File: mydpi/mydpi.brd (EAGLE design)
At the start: 40 x 20 mm, 16 parts, among them Q1 DMN3404L, U1 MEGA32U4-MU, U2 AP7381-33Y-13

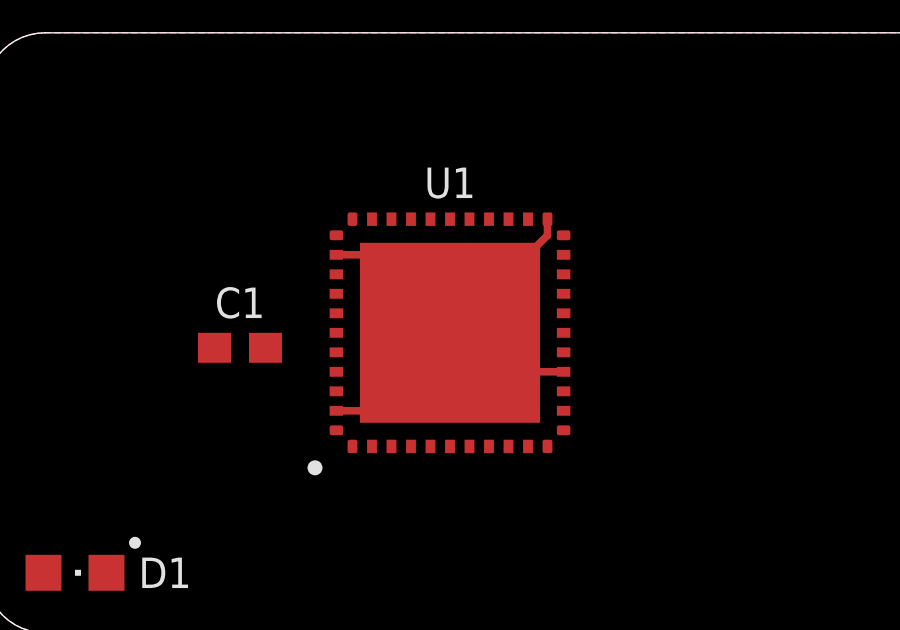
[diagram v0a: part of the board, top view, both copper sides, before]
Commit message: Added supply voltage
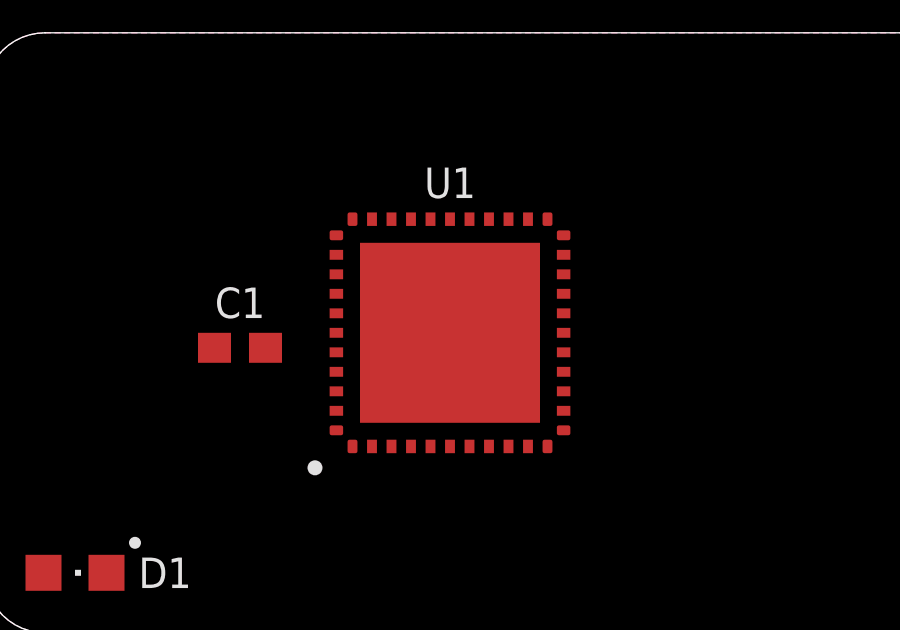
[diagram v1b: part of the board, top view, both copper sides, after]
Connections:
- new net +5V: D1.A
- new net N$1: R3.1, U1.32
- new net N$2: D1.C, R3.2
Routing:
- net GND: track 5.81 -> 0.00 mm
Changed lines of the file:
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@@
 <drawing>
 <settings>
-<setting alwaysvectorfont="yes"/>
+<setting alwaysvectorfont="no"/>
 <setting verticaltext="up"/>
 </settings>
@@
 </signal>
 <signal name="GND">
-<contactref element="U1" pad="23"/>
-<contactref element="U1" pad="15"/>
-<contactref element="U1" pad="EXP"/>
-<contactref element="U1" pad="35"/>
-<contactref element="U1" pad="43"/>
 <polygon width="0.254" layer="16">
 <vertex x="2" y="20"/>
@@
 <vertex x="0" y="18" curve="-90"/>
 </polygon>
-<wire x1="11.7125" y1="12.6" x2="12.9" y2="12.6" width="0.254" layer="1"/>
-<wire x1="12.9" y1="12.6" x2="13" y2="12.5" width="0.254" layer="1"/>
-<wire x1="11.7125" y1="7.4" x2="12.9" y2="7.4" width="0.254" layer="1"/>
-<wire x1="12.9" y1="7.4" x2="13" y2="7.5" width="0.254" layer="1"/>
-<wire x1="19.2875" y1="8.7" x2="17.8" y2="8.7" width="0.254" layer="1"/>
-<wire x1="17.8" y1="8.7" x2="17.5" y2="9" width="0.254" layer="1"/>
-<wire x1="18.75" y1="13.7875" x2="18.75" y2="13.25" width="0.254" layer="1"/>
-<wire x1="18.75" y1="13.25" x2="18.25" y2="12.75" width="0.254" layer="1"/>
 <contactref element="U2" pad="2"/>
 <contactref element="U2" pad="2@1"/>
+<contactref element="U1" pad="15"/>
+<contactref element="U1" pad="EXP"/>
+<contactref element="U1" pad="23"/>
+<contactref element="U1" pad="35"/>
+<contactref element="U1" pad="43"/>
 <wire x1="51.5" y1="3.273" x2="51.5" y2="5.94" width="0" layer="19" extent="1-1"/>
 <wire x1="19.2875" y1="8.7" x2="51.5" y2="5.94" width="0" layer="19" extent="1-1"/>
-<wire x1="15.5" y1="10" x2="17.5" y2="9" width="0" layer="19" extent="1-1"/>
-<wire x1="13" y1="12.5" x2="15.5" y2="10" width="0" layer="19" extent="1-1"/>
-<wire x1="13" y1="7.5" x2="15.5" y2="10" width="0" layer="19" extent="1-1"/>
-<wire x1="18.25" y1="12.75" x2="17.5" y2="9" width="0" layer="19" extent="1-1"/>
+<wire x1="15.5" y1="10" x2="19.2875" y2="8.7" width="0" layer="19" extent="1-1"/>
+<wire x1="11.7125" y1="12.6" x2="15.5" y2="10" width="0" layer="19" extent="1-1"/>
+<wire x1="11.7125" y1="7.4" x2="15.5" y2="10" width="0" layer="19" extent="1-1"/>
+<wire x1="18.75" y1="13.7875" x2="15.5" y2="10" width="0" layer="19" extent="1-1"/>
 </signal>
 <signal name="VCC">
@@
 <vertex x="0" y="18" curve="-90"/>
 </polygon>
+<contactref element="D1" pad="A"/>
 </signal>
 <signal name="UCAP">
@@
 <contactref element="U1" pad="4"/>
 </signal>
+<signal name="N$1">
+<contactref element="U1" pad="32"/>
+<contactref element="R3" pad="1"/>
+<wire x1="12.9" y1="13.7875" x2="41.65" y2="36" width="0" layer="19" extent="1-1"/>
+</signal>
+<signal name="N$2">
+<contactref element="R3" pad="2"/>
+<contactref element="D1" pad="C"/>
+<wire x1="4.05" y1="2" x2="43.35" y2="36" width="0" layer="19" extent="1-1"/>
+</signal>
 </signals>

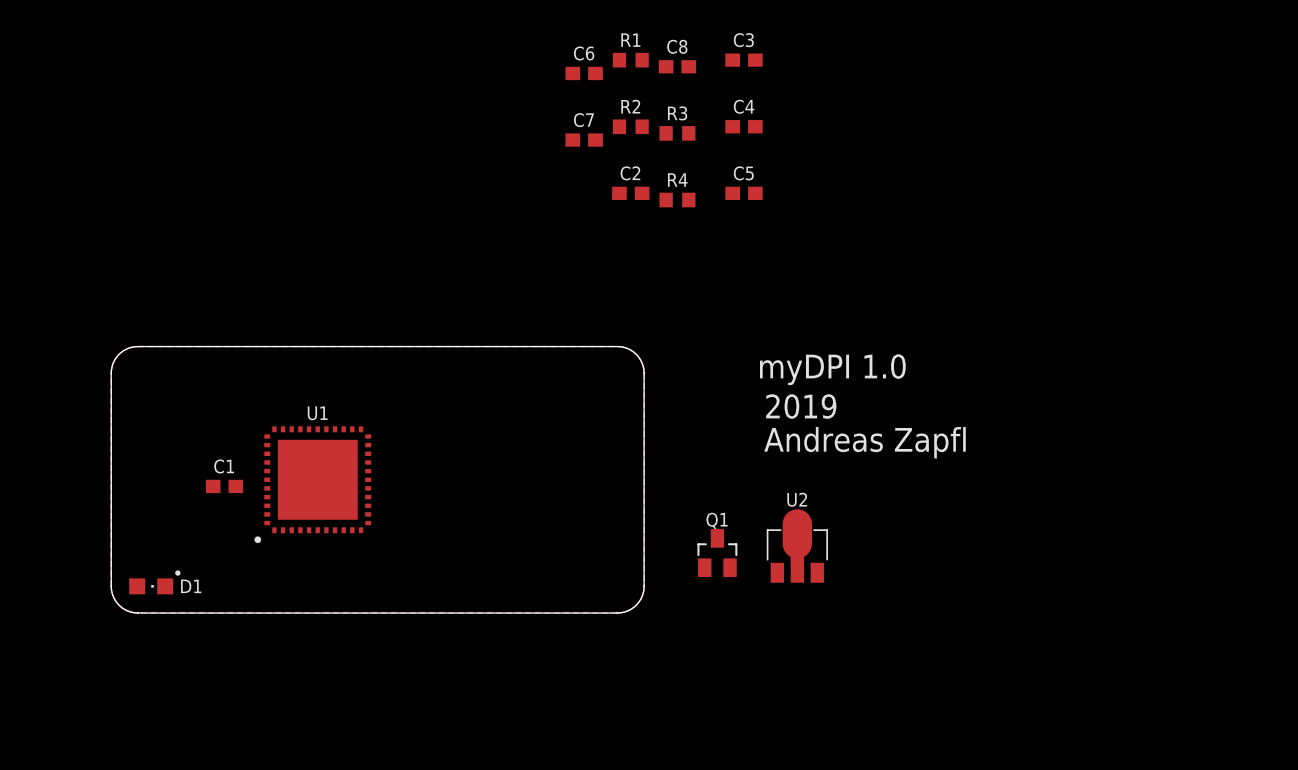
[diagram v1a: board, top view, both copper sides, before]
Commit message: CC resistors added
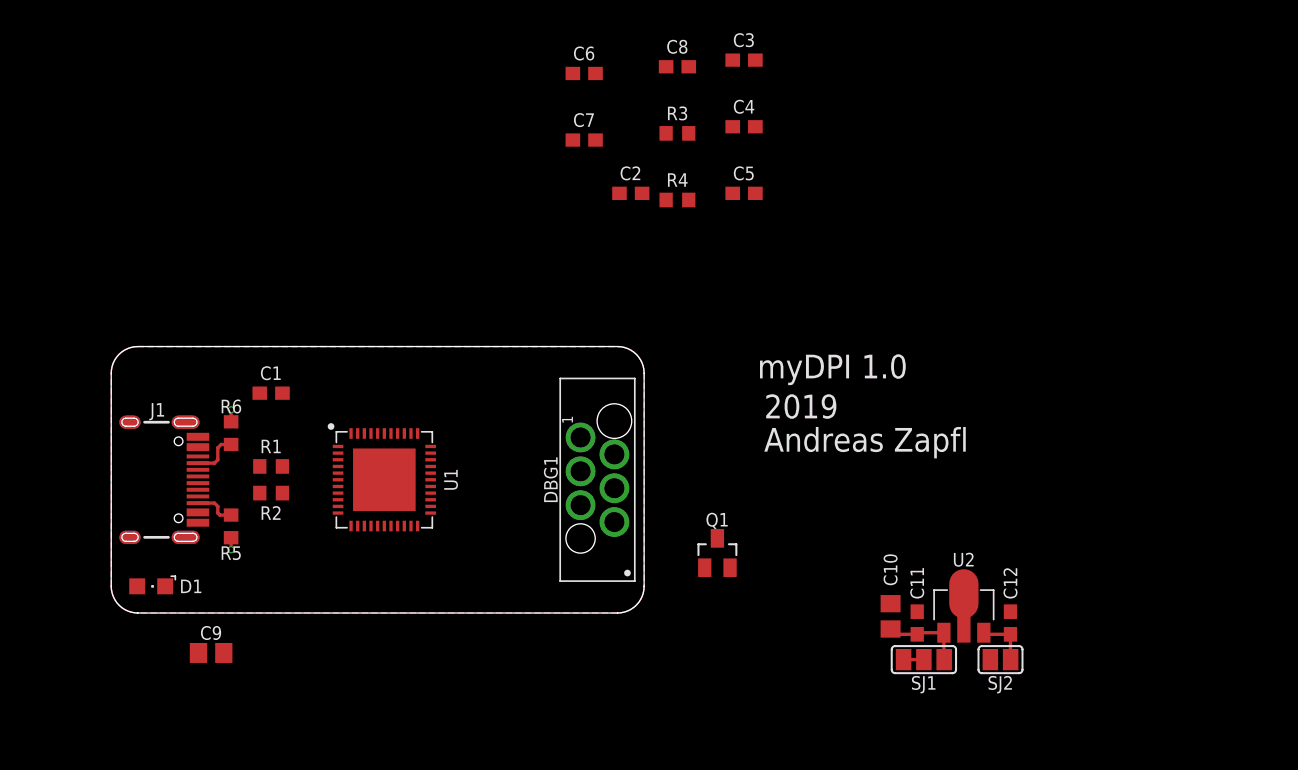
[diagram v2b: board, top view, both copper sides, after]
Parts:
- added C10, C9: 22u, zaan-Capacitors:C0805
- added C11, C12: 100n, zaan-Capacitors:C0603
- added DBG1: AVR-UPDI-SKEDD, zaan-Connectors:490107670612A
- added J1: (no value), zaan-Connectors:USB-C-16P
- added R5, R6: 5.1k, zaan-Resistors:R0603
- added SJ1: (no value), jumper:SJ_2
- added SJ2: (no value), jumper:SJ
- U1: device zaan-IC-Microcontroller:QFN44ML8X8 -> zaan-IC-Microcontroller:TQFN44_7MM
- moved R1 40.7 mm to (12.0, 11.0)
- moved R2 38.5 mm to (12.0, 9.00)
- moved U2 13.3 mm to (64.0, 0.50)
- moved C1 7.83 mm to (12.0, 16.5)
- moved U1 5.00 mm to (20.5, 10.0), turned to 0 degrees
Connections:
- new net +3V3: C10.1, C11.1, SJ1.1, U2.1
- new net MEDBG_UPDI: DBG1.3, U1.1
- new net MEDBG_VTG: DBG1.4, SJ1.2
- new net N$4: C12.1, SJ2.2, U2.3
- new net N$5: J1.B5, R5.2
- new net N$6: J1.A5, R6.2
- new net USB_N: J1.A7, J1.B7, R1.1
- new net USB_P: J1.A6, J1.B6, R2.1
- net +5V: now also J1.VBUS1, J1.VBUS2, SJ1.3, SJ2.1
- net D_N: now also R1.2
- net D_P: now also R2.2
- net GND: now also C10.2, C11.2, C12.2, DBG1.2, J1.GND, J1.GND2, R5.1, R6.1
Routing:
- net +3V3: track 0.00 -> 6.24 mm
- net N$4: track 0.00 -> 3.96 mm
- net N$6: track 0.00 -> 3.60 mm
- net N$5: track 0.00 -> 3.16 mm
- net GND: track 0.00 -> 1.80 mm, vias 0 -> 2
- net N$3: track 0.00 -> 1.50 mm

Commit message: Placement LDO, Caps
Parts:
- removed C8: 1n, zaan-Capacitors:C0603
- removed R4: 1k, zaan-Resistors:R0603
- removed SJ2: (no value), jumper:SJ
- added C13: 100n, zaan-Capacitors:C0603
- added D2: LTST-C171KSKT, zaan-Optoelectronics:CHIPLED_0805
- added ICSP1: AVR-ISP-1.27MM, zaan-Connectors:AVRISP-1.27
- added R7, R8: 100k, zaan-Resistors:R0603
- added R9: 1k, zaan-Resistors:R0603
- C6: value 1n -> 100n
- moved C9 77.9 mm to (72.5, 40.0)
- moved Q1 44.9 mm to (77.5, 36.0)
- moved C12 43.8 mm to (24.0, 4.75), flipped to the bottom, turned to 180 degrees
- moved U2 40.1 mm to (24.8, 8.75), flipped to the bottom
- moved C3 39.0 mm to (18.0, 16.0)
- moved C4 36.2 mm to (26.5, 7.00), turned to 270 degrees
- moved C11 33.3 mm to (28.2, 7.50), flipped to the bottom
- moved C2 31.6 mm to (22.5, 4.50), turned to 180 degrees
- moved D1 31.4 mm to (32.0, 14.0), turned to 0 degrees
- moved C6 31.2 mm to (32.0, 9.50), turned to 90 degrees
- moved C10 29.4 mm to (30.2, 8.00), flipped to the bottom
- moved SJ1 29.3 mm to (32.5, 3.50), flipped to the bottom, turned to 270 degrees
- moved C7 29.2 mm to (32.0, 6.50), turned to 90 degrees
- moved C5 28.6 mm to (23.5, 16.0), turned to 180 degrees
- moved R3 25.2 mm to (30.2, 14.0), turned to 90 degrees
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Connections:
- removed net AREF: U1.42
- removed net AVCC: U1.24, U1.44
- removed net N$4: C12.1, SJ2.2, U2.3
- removed net UCAP: U1.6
- removed net UGND: U1.5
- removed net UVCC: U1.2
- removed net VBUS: U1.7
- removed net VCC: U1.14, U1.34
- new net N$13: U1.17
- new net N$14: U1.16
- new net N$7: R7.1, U1.33
- new net N$8: C1.1, U1.6
- new net N$9: D2.A, R9.2
- new net PDI: ICSP1.4, U1.10
- new net PDO: ICSP1.1, U1.11
- new net RST: C13.1, ICSP1.5, R8.1, U1.13
- new net SCK: ICSP1.3, U1.9
- net +5V: now also C12.1, C2.1, C3.1, C4.1, C5.1, C6.1, C7.1, ICSP1.2, R7.2, R8.2, R9.1, U1.14, U1.2, U1.24, U1.34, U1.42, U1.44, U1.7, U2.3; no longer SJ2.1
- net D_N: now also R2.2; no longer R1.2
- net D_P: now also R1.2; no longer R2.2
- net GND: now also C1.2, C13.2, C2.2, C3.2, C4.2, C5.2, C6.2, C7.2, D2.C, ICSP1.6, U1.5
- net USB_N: now also R2.1; no longer R1.1
- net USB_P: now also R1.1; no longer R2.1
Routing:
- net MEDBG_VTG: track 0.00 -> 12.4 mm
- net +5V: track 0.00 -> 9.10 mm, vias 0 -> 3
- net N$4: track 3.96 -> 0.00 mm
- net GND: track 1.80 -> 5.18 mm, vias 2 -> 5
- net N$9: track 0.00 -> 2.08 mm
- net +3V3: track 6.24 -> 8.05 mm
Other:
- board text added: "3V3"
- board text added: "5V"
- board text added: "Target"

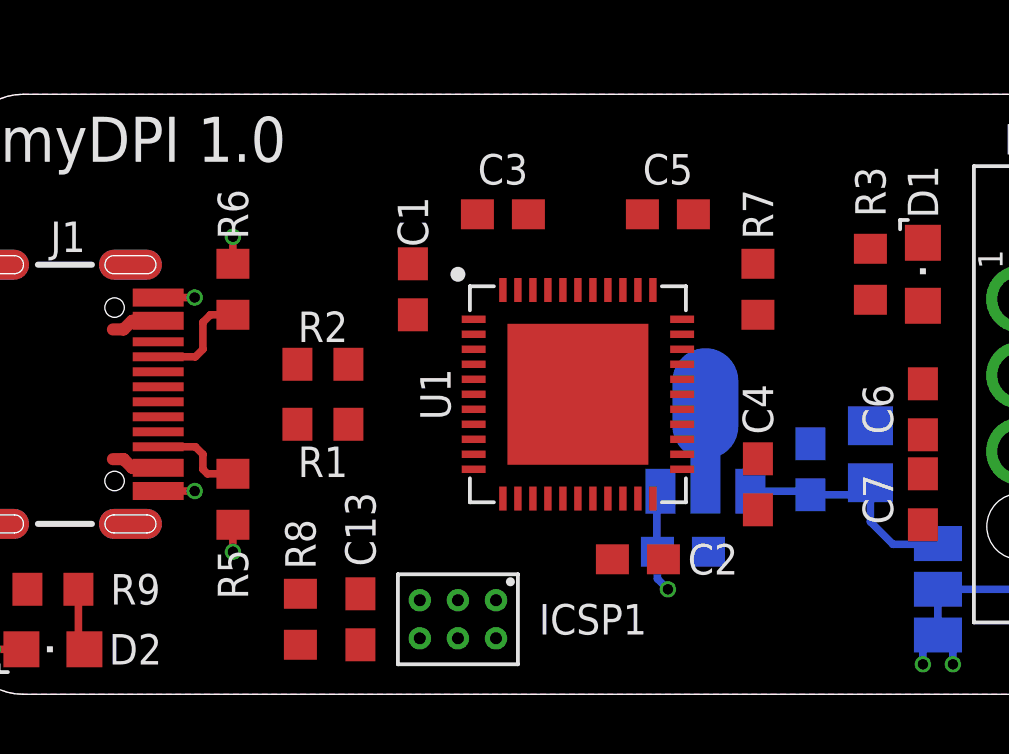
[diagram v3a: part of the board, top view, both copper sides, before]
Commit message: Crystal Added
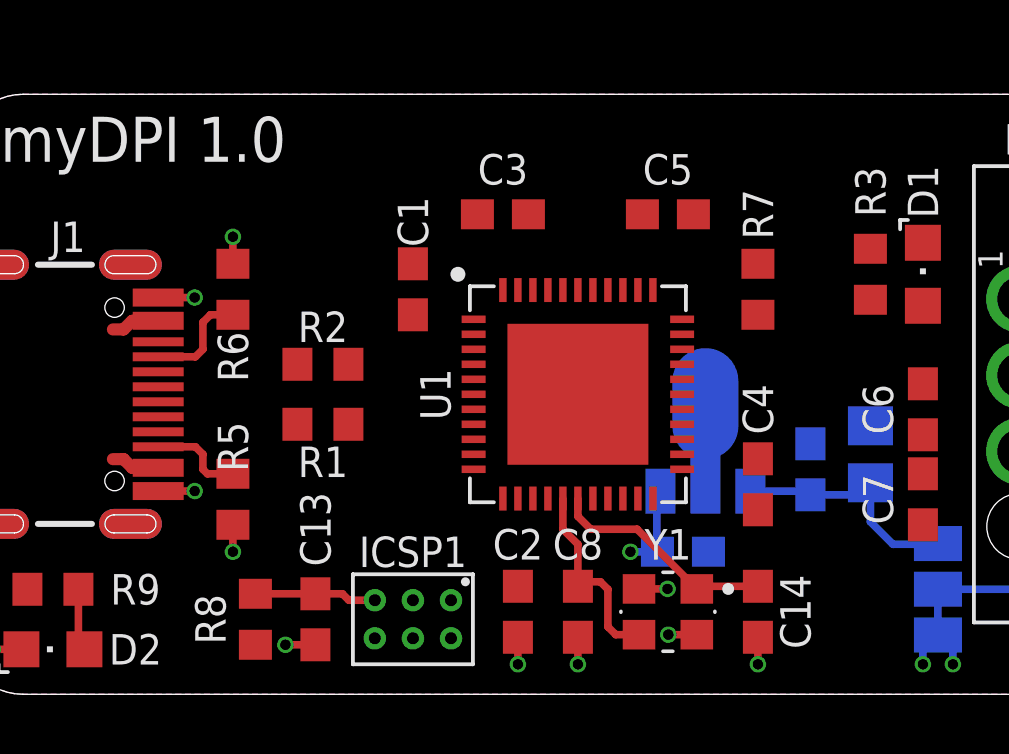
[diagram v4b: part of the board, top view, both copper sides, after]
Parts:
- added C14, C8: 12p, zaan-Capacitors:C0603
- added Y1: 830069392, zaan-Electromechanical:WE-XTAL_CFPX-218
- moved C2 4.37 mm to (18.5, 2.75), turned to 270 degrees
- moved C13 1.50 mm to (11.8, 2.50)
- moved ICSP1 1.50 mm to (15.0, 2.50)
- moved R8 1.50 mm to (9.75, 2.50)
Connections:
- removed net N$13: U1.17
- removed net N$14: U1.16
- new net XTAL1: C14.1, U1.17, Y1.1
- new net XTAL2: C8.1, U1.16, Y1.3
- net GND: now also C14.2, C8.2, Y1.2, Y1.4
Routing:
- net XTAL1: track 0.00 -> 7.77 mm
- net XTAL2: track 0.00 -> 6.63 mm
- net GND: track 5.18 -> 10.8 mm, vias 5 -> 11
- net RST: track 0.00 -> 4.07 mm

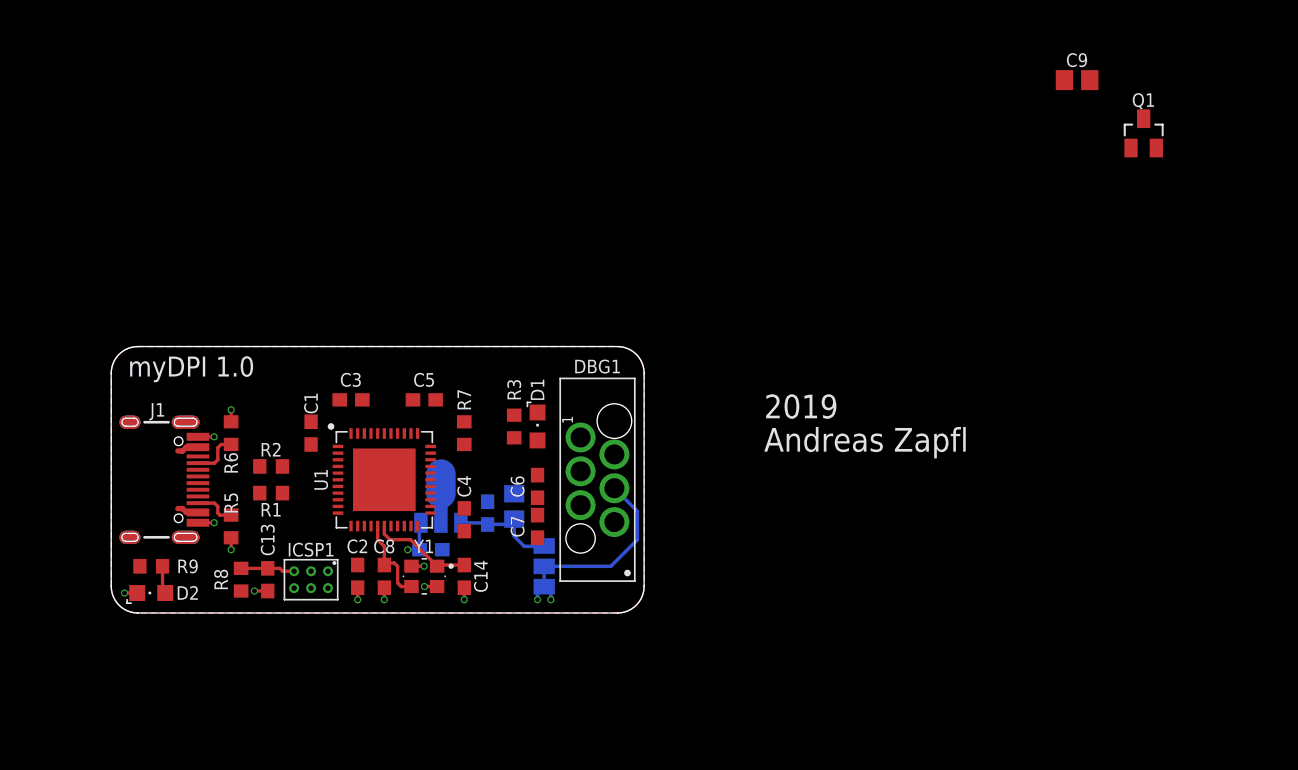
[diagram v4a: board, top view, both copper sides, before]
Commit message: Added Reset Switch
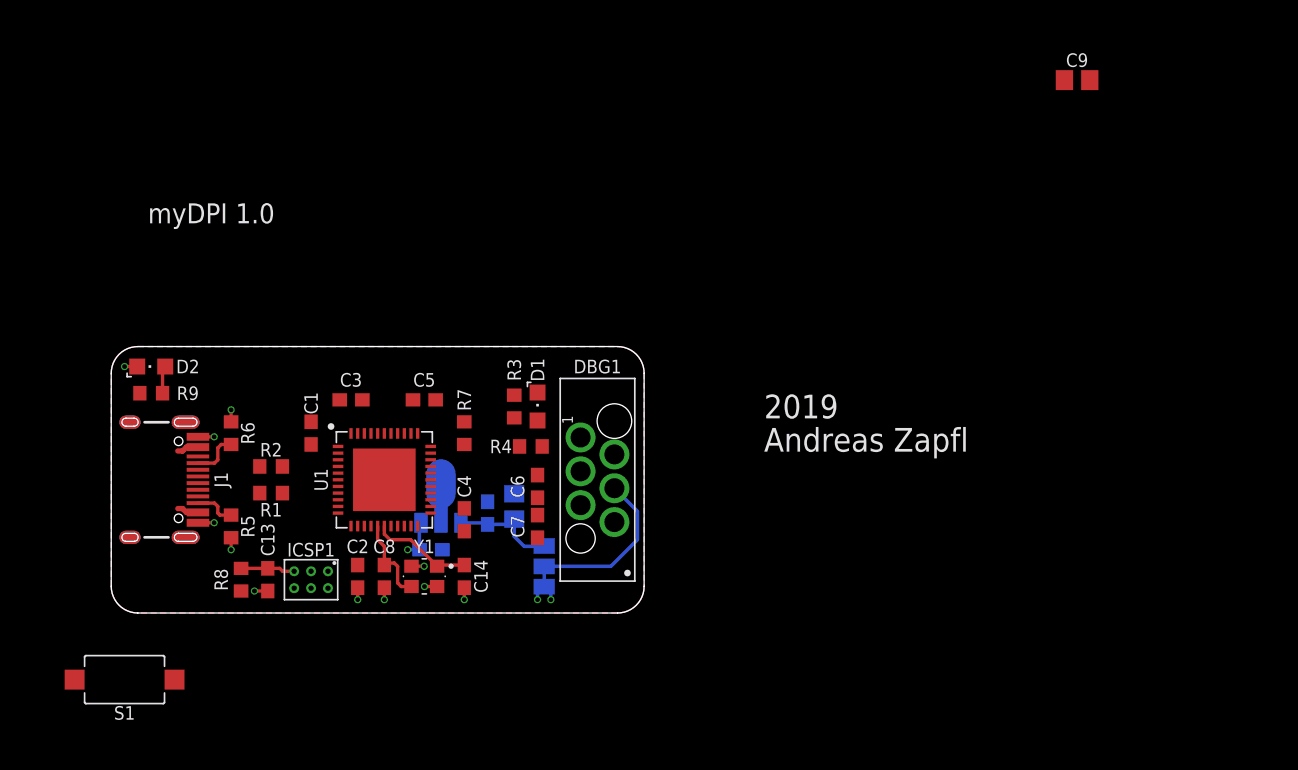
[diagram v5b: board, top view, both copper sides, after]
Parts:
- removed Q1: DMN3404L, zaan-Discrete:SOT23
- added R4: 1k, zaan-Resistors:R0603
- added S1: TS-1101-C-W, zaan-Electromechanical:SPST-6X3.6
- DBG1: device zaan-Connectors:490107670612A -> zaan-Connectors:490107670612
- moved D2 17.0 mm to (3.00, 18.5)
- moved R9 13.0 mm to (3.00, 16.5)
- moved D1 1.50 mm to (32.0, 15.5)
- moved R3 1.50 mm to (30.2, 15.5)
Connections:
- new net PE6: R4.1, U1.1
- net MEDBG_UPDI: now also R4.2; no longer U1.1
